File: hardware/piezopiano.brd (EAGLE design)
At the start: 90 x 99.8 mm, 76 parts, among them J1 CON2, J4 JST-PH-2-SMT-SE, Q1 DMN3404L, Q2 DMN3404L, Q3 DMN3404L, Q4 DMN3404L, Q5 DMN3404L, Q6 DMN3404L, Q7 DMN3404L, Q8 DMN3404L, U1 ATMEGA4809, U2 CH340E_MSOP10, U3 TP4333

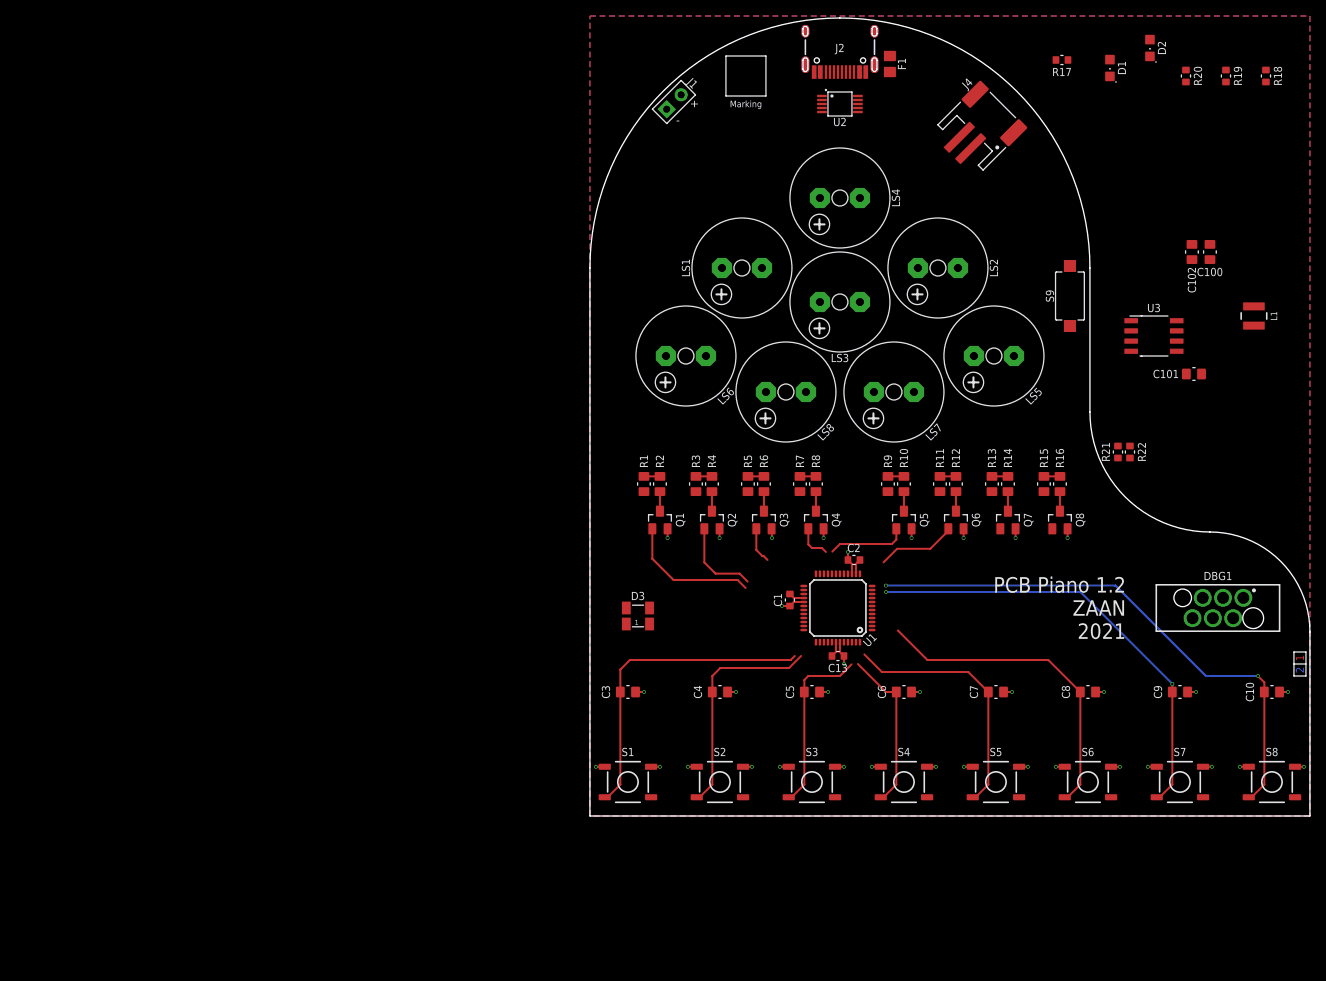
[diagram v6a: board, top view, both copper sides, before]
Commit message: Added proto area
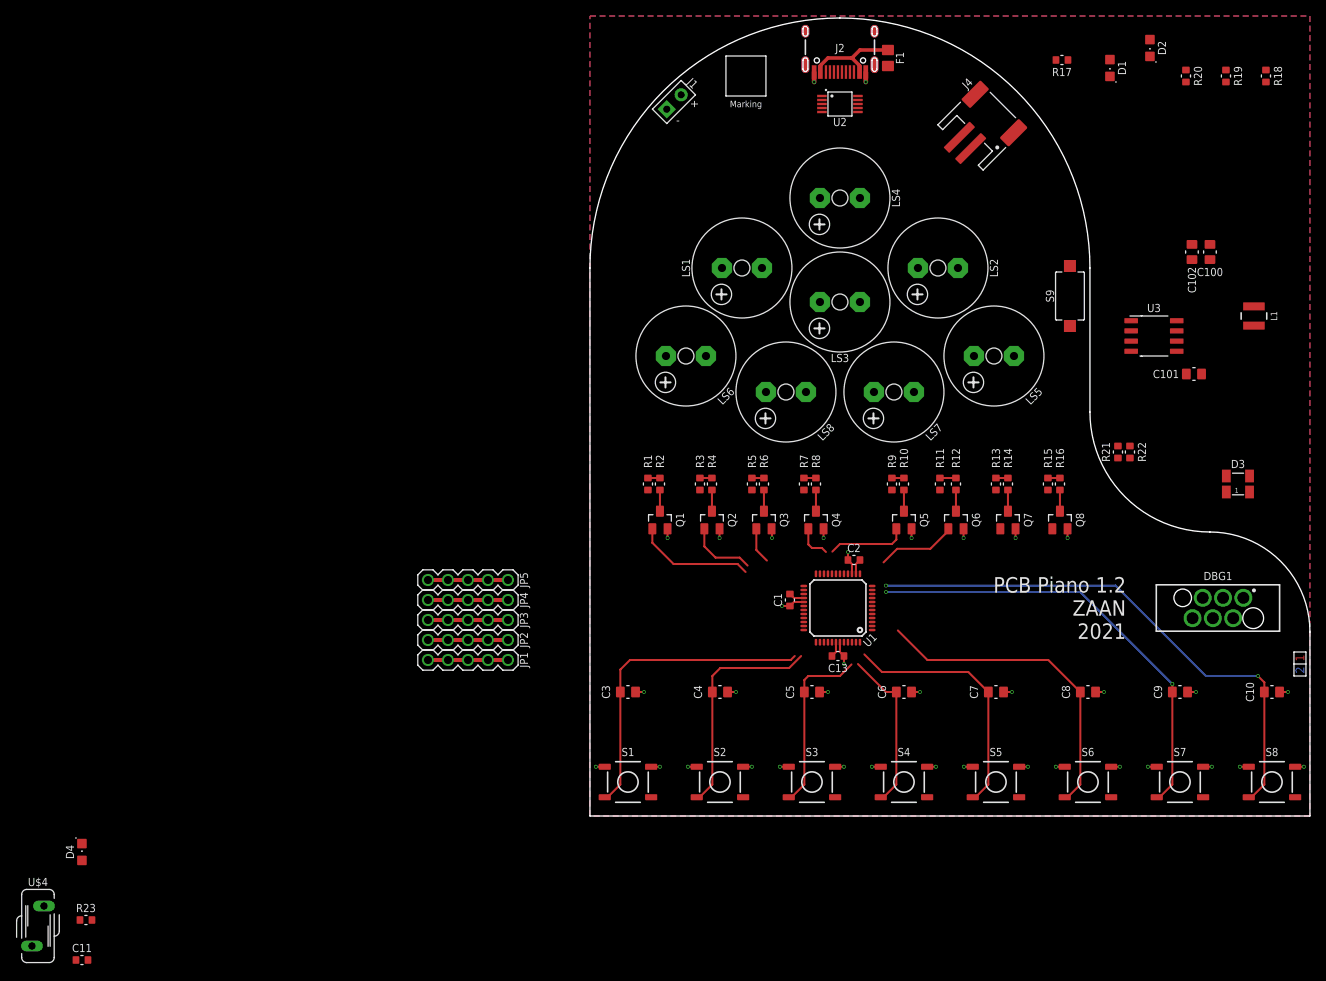
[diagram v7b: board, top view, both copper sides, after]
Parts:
- added C11: 100n, zaan-Capacitors:C0603
- added D4: LTST-C171KSKT, zaan-Optoelectronics:CHIPLED_0805
- added JP1, JP2, JP3, JP4, JP5: PINROW-1X5, zaan-No-Category:1X01
- added R23: 1k, zaan-Resistors:R0603
- added U$4: 820572711, zaan-No-Category:S07K150
- R1, R10, R11, R12, R13, R14, R15, R16, R2, R3, R4, R5, R6, R7, R8, R9: device zaan-Resistors:R0805 -> zaan-Resistors:R0603
- moved D3 76.8 mm to (81.0, 41.5)
- moved F1 0.79 mm to (37.2, 94.8)
- moved R1 0.50 mm to (7.25, 41.5)
- moved R13 0.50 mm to (50.8, 41.5)
- moved R15 0.50 mm to (57.2, 41.5)
- moved R3 0.50 mm to (13.8, 41.5)
- moved R5 0.50 mm to (20.2, 41.5)
- moved R7 0.50 mm to (26.8, 41.5)
- moved R9 0.50 mm to (37.8, 41.5)
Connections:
- new net N$19: R23.1, U2.6
- new net N$20: D4.A, R23.2
- new net V3: C11.1, U2.10
- net GND: now also C11.2, D4.C
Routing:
- net VBUS: track 0.00 -> 12.2 mm
- net GND: track 44.0 -> 46.5 mm, vias 35 -> 37
- net D4: track 16.9 -> 14.9 mm
- net D3: track 10.6 -> 8.60 mm
- net N$4: track 2.00 -> 1.50 mm
- net N$18: track 2.00 -> 1.50 mm
- net N$16: track 2.00 -> 1.50 mm
- net N$15: track 2.00 -> 1.50 mm
- net N$13: track 2.00 -> 1.50 mm
- net N$11: track 2.00 -> 1.50 mm
- net N$10: track 2.00 -> 1.50 mm
